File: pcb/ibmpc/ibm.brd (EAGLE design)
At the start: 104 x 74 mm, 40 parts, among them J2 ATX24RH

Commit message: working on new version
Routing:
- net N$3: track 133.6 -> 132.5 mm
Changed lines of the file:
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@@
 <layer number="14" name="Route14" color="22" fill="1" visible="no" active="no"/>
 <layer number="15" name="Route15" color="23" fill="1" visible="no" active="no"/>
-<layer number="16" name="Bottom" color="1" fill="1" visible="yes" active="yes"/>
+<layer number="16" name="Bottom" color="1" fill="1" visible="no" active="yes"/>
 <layer number="17" name="Pads" color="2" fill="1" visible="yes" active="yes"/>
 <layer number="18" name="Vias" color="2" fill="1" visible="yes" active="yes"/>
@@
 <layer number="22" name="bPlace" color="7" fill="1" visible="no" active="yes"/>
 <layer number="23" name="tOrigins" color="15" fill="1" visible="yes" active="yes"/>
-<layer number="24" name="bOrigins" color="15" fill="1" visible="yes" active="yes"/>
+<layer number="24" name="bOrigins" color="15" fill="1" visible="no" active="yes"/>
 <layer number="25" name="tNames" color="7" fill="1" visible="no" active="yes"/>
 <layer number="26" name="bNames" color="7" fill="1" visible="no" active="yes"/>
@@
 <layer number="38" name="bTest" color="7" fill="1" visible="no" active="yes"/>
 <layer number="39" name="tKeepout" color="4" fill="11" visible="yes" active="yes"/>
-<layer number="40" name="bKeepout" color="1" fill="11" visible="yes" active="yes"/>
+<layer number="40" name="bKeepout" color="1" fill="11" visible="no" active="yes"/>
 <layer number="41" name="tRestrict" color="4" fill="10" visible="yes" active="yes"/>
-<layer number="42" name="bRestrict" color="1" fill="10" visible="yes" active="yes"/>
+<layer number="42" name="bRestrict" color="1" fill="10" visible="no" active="yes"/>
 <layer number="43" name="vRestrict" color="2" fill="10" visible="no" active="yes"/>
 <layer number="44" name="Drills" color="7" fill="1" visible="no" active="yes"/>
@@
 <wire x1="94.234" y1="45.212" x2="94.234" y2="51.435" width="0.3048" layer="16"/>
 <wire x1="92.642" y1="43.62" x2="94.234" y2="45.212" width="0.3048" layer="16"/>
-<wire x1="88.821" y1="64.446" x2="88.821" y2="63.452" width="0.3048" layer="16"/>
-<wire x1="88.821" y1="63.452" x2="90.424" y2="61.849" width="0.3048" layer="16"/>
-<wire x1="90.424" y1="61.849" x2="92.456" y2="61.849" width="0.3048" layer="16"/>
-<wire x1="94.234" y1="60.071" x2="94.234" y2="51.435" width="0.3048" layer="16"/>
-<wire x1="92.456" y1="61.849" x2="94.234" y2="60.071" width="0.3048" layer="16"/>
+<wire x1="88.821" y1="64.446" x2="88.821" y2="63.706" width="0.3048" layer="16"/>
+<wire x1="94.234" y1="58.293" x2="94.234" y2="51.435" width="0.3048" layer="16"/>
+<wire x1="88.821" y1="63.706" x2="94.234" y2="58.293" width="0.3048" layer="16"/>
 <wire x1="43.688" y1="52.451" x2="77.089" y2="52.451" width="0.3048" layer="16"/>
 <wire x1="77.089" y1="52.451" x2="78.105" y2="51.435" width="0.3048" layer="16"/>

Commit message: working on new version
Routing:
- net GND: track 63.2 -> 62.2 mm
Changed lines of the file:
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@@
 <layer number="14" name="Route14" color="22" fill="1" visible="no" active="no"/>
 <layer number="15" name="Route15" color="23" fill="1" visible="no" active="no"/>
-<layer number="16" name="Bottom" color="1" fill="1" visible="no" active="yes"/>
+<layer number="16" name="Bottom" color="1" fill="1" visible="yes" active="yes"/>
 <layer number="17" name="Pads" color="2" fill="1" visible="yes" active="yes"/>
 <layer number="18" name="Vias" color="2" fill="1" visible="yes" active="yes"/>
 <layer number="19" name="Unrouted" color="6" fill="1" visible="yes" active="yes"/>
 <layer number="20" name="Dimension" color="24" fill="1" visible="yes" active="yes"/>
-<layer number="21" name="tPlace" color="7" fill="1" visible="no" active="yes"/>
-<layer number="22" name="bPlace" color="7" fill="1" visible="no" active="yes"/>
+<layer number="21" name="tPlace" color="7" fill="1" visible="yes" active="yes"/>
+<layer number="22" name="bPlace" color="7" fill="1" visible="yes" active="yes"/>
 <layer number="23" name="tOrigins" color="15" fill="1" visible="yes" active="yes"/>
-<layer number="24" name="bOrigins" color="15" fill="1" visible="no" active="yes"/>
-<layer number="25" name="tNames" color="7" fill="1" visible="no" active="yes"/>
-<layer number="26" name="bNames" color="7" fill="1" visible="no" active="yes"/>
-<layer number="27" name="tValues" color="7" fill="1" visible="no" active="yes"/>
-<layer number="28" name="bValues" color="7" fill="1" visible="no" active="yes"/>
+<layer number="24" name="bOrigins" color="15" fill="1" visible="yes" active="yes"/>
+<layer number="25" name="tNames" color="7" fill="1" visible="yes" active="yes"/>
+<layer number="26" name="bNames" color="7" fill="1" visible="yes" active="yes"/>
+<layer number="27" name="tValues" color="7" fill="1" visible="yes" active="yes"/>
+<layer number="28" name="bValues" color="7" fill="1" visible="yes" active="yes"/>
 <layer number="29" name="tStop" color="7" fill="3" visible="no" active="yes"/>
 <layer number="30" name="bStop" color="7" fill="6" visible="no" active="yes"/>
@@
 <layer number="38" name="bTest" color="7" fill="1" visible="no" active="yes"/>
 <layer number="39" name="tKeepout" color="4" fill="11" visible="yes" active="yes"/>
-<layer number="40" name="bKeepout" color="1" fill="11" visible="no" active="yes"/>
+<layer number="40" name="bKeepout" color="1" fill="11" visible="yes" active="yes"/>
 <layer number="41" name="tRestrict" color="4" fill="10" visible="yes" active="yes"/>
-<layer number="42" name="bRestrict" color="1" fill="10" visible="no" active="yes"/>
+<layer number="42" name="bRestrict" color="1" fill="10" visible="yes" active="yes"/>
 <layer number="43" name="vRestrict" color="2" fill="10" visible="no" active="yes"/>
 <layer number="44" name="Drills" color="7" fill="1" visible="no" active="yes"/>
@@
 <layer number="49" name="Reference" color="7" fill="1" visible="no" active="yes"/>
 <layer number="50" name="dxf" color="7" fill="1" visible="no" active="no"/>
-<layer number="51" name="tDocu" color="7" fill="1" visible="no" active="yes"/>
-<layer number="52" name="bDocu" color="7" fill="1" visible="no" active="yes"/>
+<layer number="51" name="tDocu" color="7" fill="1" visible="yes" active="yes"/>
+<layer number="52" name="bDocu" color="7" fill="1" visible="yes" active="yes"/>
 <layer number="53" name="tGND_GNDA" color="7" fill="1" visible="no" active="no"/>
 <layer number="54" name="bGND_GNDA" color="7" fill="1" visible="no" active="no"/>
@@
 <wire x1="104" y1="10.795" x2="100.825" y2="7.62" width="0" layer="20" curve="-90"/>
 <wire x1="100.825" y1="7.62" x2="81" y2="7.62" width="0" layer="20"/>
-<text x="41.3926" y="4.0764" size="2.54" layer="25" distance="35" align="center">IBM PC PicoPSU Adaptor
+<text x="73.2696" y="12.9664" size="2.54" layer="25" distance="35" align="center">IBM PC PicoPSU Adaptor
 dekuNukem 2023</text>
 <text x="83.608" y="45.184" size="2.54" layer="25" rot="R180" align="center">GND</text>
 <text x="34.218" y="71.93" size="2.1844" layer="25" distance="35" align="center">FUSE 7.5A MAX</text>
-<text x="52.3746" y="22.3784" size="3.175" layer="25" distance="35" align="center">picoRC.com</text>
+<text x="53.0096" y="22.1244" size="3.175" layer="25" distance="35" align="center">picoRC.com</text>
 <text x="38.529" y="26.012" size="1.4224" layer="25" align="center">GND</text>
 <text x="38.275" y="23.615" size="1.4224" layer="25" align="center">-12</text>
@@
 </element>
 <element name="C17" library="capacitor-wima" library_urn="urn:adsk.eagle:library:116" package="C5B2.5" package3d_urn="urn:adsk.eagle:package:5426/1" value="" x="35.733" y="34.474" smashed="yes" rot="R180">
-<attribute name="NAME" x="31.947" y="31.796" size="1.27" layer="25" ratio="10"/>
+<attribute name="NAME" x="31.947" y="31.542" size="1.27" layer="25" ratio="10"/>
 <attribute name="POPULARITY" value="10" x="35.733" y="34.474" size="1.778" layer="27" rot="R180" display="off"/>
 <attribute name="VALUE" x="37.765" y="37.268" size="1.27" layer="27" ratio="10" rot="R180"/>
@@
 <via x="2.413" y="11.43" extent="1-16" drill="1"/>
 <via x="2.413" y="9.398" extent="1-16" drill="1"/>
-<wire x1="2.413" y1="11.43" x2="2.413" y2="9.398" width="2.54" layer="16"/>
-<wire x1="2.413" y1="9.398" x2="2.413" y2="8.382" width="2.54" layer="16"/>
-<wire x1="2.387" y1="4" x2="2.387" y2="7.594" width="1.016" layer="16"/>
-<wire x1="2.387" y1="7.594" x2="2.413" y2="7.62" width="1.016" layer="16"/>
-<wire x1="2.413" y1="7.62" x2="2.413" y2="9.398" width="1.016" layer="16"/>
 <contactref element="C12" pad="-"/>
 <contactref element="C13" pad="2"/>
@@
 <vertex x="10.668" y="14.224"/>
 </polygon>
+<wire x1="2.413" y1="11.43" x2="2.413" y2="9.398" width="2.54" layer="16"/>
+<wire x1="2.387" y1="4" x2="2.387" y2="9.372" width="1.524" layer="16"/>
+<wire x1="2.387" y1="9.372" x2="2.413" y2="9.398" width="1.524" layer="16"/>
 </signal>
 <signal name="+5V">

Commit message: working on new version
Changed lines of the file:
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@@
 <text x="83.608" y="45.184" size="2.54" layer="25" rot="R180" align="center">GND</text>
 <text x="34.218" y="71.93" size="2.1844" layer="25" distance="35" align="center">FUSE 7.5A MAX</text>
-<text x="53.0096" y="22.1244" size="3.175" layer="25" distance="35" align="center">picoRC.com</text>
+<text x="25.1966" y="11.2024" size="3.175" layer="25" distance="35" align="center">picoRC.com</text>
 <text x="38.529" y="26.012" size="1.4224" layer="25" align="center">GND</text>
 <text x="38.275" y="23.615" size="1.4224" layer="25" align="center">-12</text>

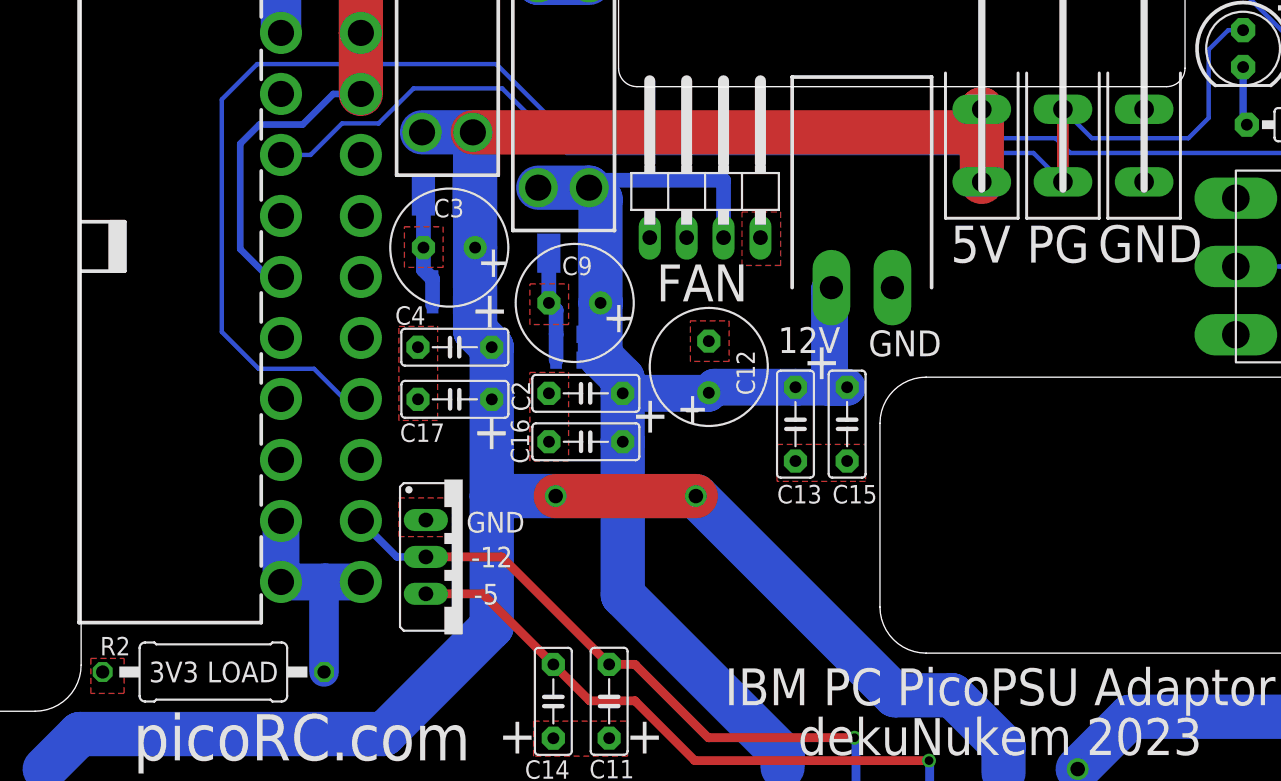
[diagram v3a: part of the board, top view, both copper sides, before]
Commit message: added 12V load resistor and blade
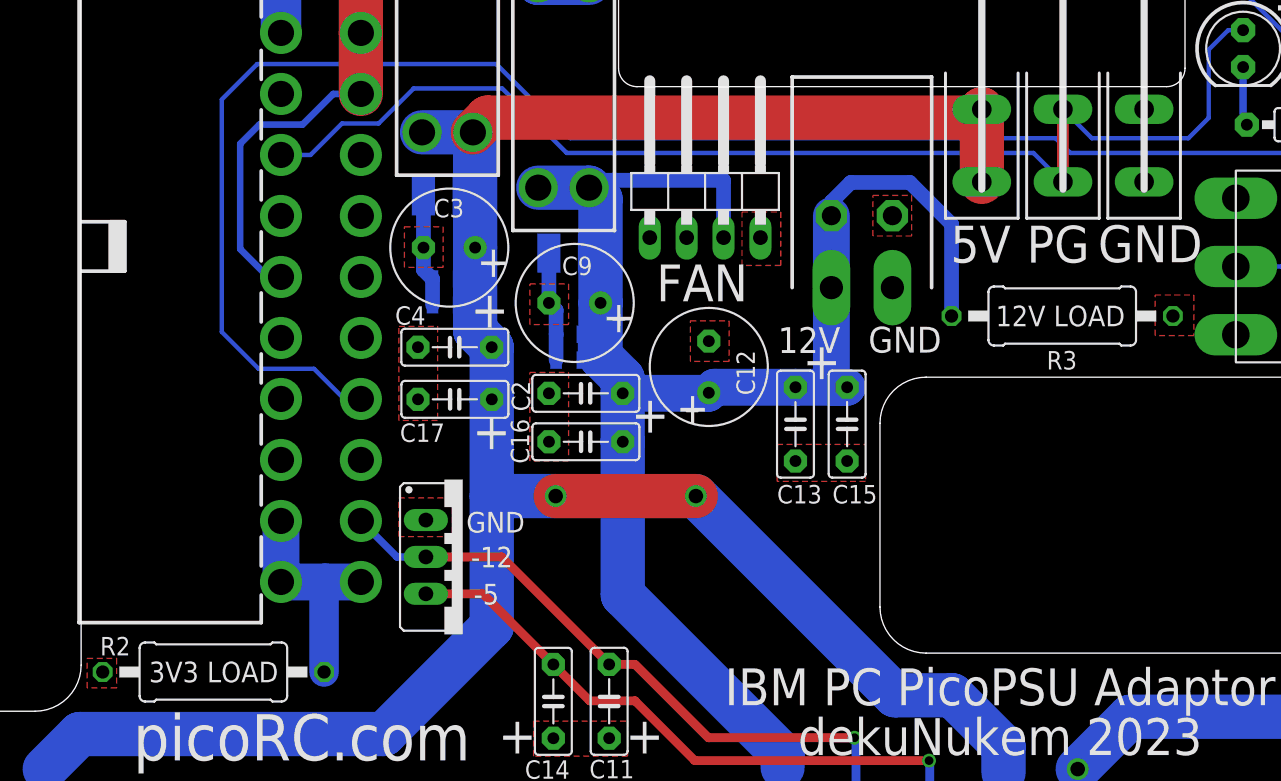
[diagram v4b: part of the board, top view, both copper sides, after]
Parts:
- added R3: (no value), adafruit_changed:0411/15
- added TP1, TP2: TPPAD1-13, testpad:P1-13
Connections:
- net +12V: now also R3.2, TP2.TP
- net GND: now also R3.1, TP1.TP
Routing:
- net +12V: track 99.4 -> 121.4 mm
- net +5V: track 176.9 -> 176.3 mm
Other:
- board text added: "12V LOAD"
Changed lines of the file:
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@@
 <text x="52.753" y="42.49" size="2.54" layer="25" align="center">FAN</text>
 <text x="60.119" y="38.553" size="1.778" layer="25" align="center">12V</text>
-<text x="66.717" y="38.326" size="1.778" layer="25" rot="R180" align="center">GND</text>
+<text x="66.717" y="38.58" size="1.778" layer="25" rot="R180" align="center">GND</text>
 <rectangle x1="69.469" y1="48.006" x2="74.549" y2="55.753" layer="41"/>
 <rectangle x1="75.184" y1="48.006" x2="80.264" y2="55.753" layer="41"/>
@@
 <text x="47.019" y="40.185" size="2.1844" layer="25" align="center">+</text>
 <text x="38.383" y="43.995" size="2.1844" layer="25" align="center">+</text>
+<text x="77.416" y="40.212" size="1.4224" layer="25" rot="R180" align="center">12V LOAD</text>
 </plain>
 <attributes>
@@
 <attribute name="VALUE" x="59.944" y="34.798" size="1.27" layer="27" ratio="10" rot="R270"/>
 </element>
+<element name="R3" library="adafruit_changed" package="0411/15" value="" x="77.548" y="40.21" smashed="yes" rot="R180">
+<attribute name="NAME" x="78.564" y="37.797" size="1.27" layer="25" ratio="10" rot="R180"/>
+<attribute name="VALUE" x="81.1294" y="40.845" size="1.27" layer="27" ratio="10" rot="R180"/>
+</element>
+<element name="TP2" library="testpad" library_urn="urn:adsk.eagle:library:385" package="P1-13" package3d_urn="urn:adsk.eagle:package:27946/1" value="TPPAD1-13" x="61.654" y="47.117" smashed="yes">
+<attribute name="POPULARITY" value="12" x="61.654" y="47.117" size="1.778" layer="27" display="off"/>
+<attribute name="TP_SIGNAL_NAME" value="" x="61.654" y="47.117" size="1.778" layer="27" display="off"/>
+</element>
+<element name="TP1" library="testpad" library_urn="urn:adsk.eagle:library:385" package="P1-13" package3d_urn="urn:adsk.eagle:package:27946/1" value="TPPAD1-13" x="65.854" y="47.117" smashed="yes">
+<attribute name="POPULARITY" value="12" x="65.854" y="47.117" size="1.778" layer="27" display="off"/>
+<attribute name="TP_SIGNAL_NAME" value="" x="65.854" y="47.117" size="1.778" layer="27" display="off"/>
+</element>
 </elements>
 <signals>
@@
 </polygon>
 <polygon width="0.1524" layer="1" thermals="no">
-<vertex x="10.668" y="16.637"/>
-<vertex x="12.954" y="16.637"/>
-<vertex x="12.954" y="14.224"/>
-<vertex x="10.668" y="14.224"/>
+<vertex x="10.414" y="16.637"/>
+<vertex x="12.446" y="16.637"/>
+<vertex x="12.446" y="14.605"/>
+<vertex x="10.414" y="14.605"/>
 </polygon>
 <wire x1="2.413" y1="11.43" x2="2.413" y2="9.398" width="2.54" layer="16"/>
 <wire x1="2.387" y1="4" x2="2.387" y2="9.372" width="1.524" layer="16"/>
 <wire x1="2.387" y1="9.372" x2="2.413" y2="9.398" width="1.524" layer="16"/>
+<contactref element="R3" pad="1"/>
+<contactref element="TP1" pad="TP"/>
+<polygon width="0.1524" layer="1" thermals="no">
+<vertex x="64.516" y="48.514"/>
+<vertex x="67.183" y="48.514"/>
+<vertex x="67.183" y="45.72"/>
+<vertex x="64.516" y="45.72"/>
+</polygon>
+<polygon width="0.1524" layer="1" thermals="no">
+<vertex x="83.947" y="41.656"/>
+<vertex x="86.614" y="41.656"/>
+<vertex x="86.614" y="38.862"/>
+<vertex x="83.947" y="38.862"/>
+</polygon>
 </signal>
 <signal name="+5V">
@@
 <wire x1="7.493" y1="9.017" x2="7.493" y2="4.026" width="1.27" layer="16"/>
 <wire x1="7.493" y1="4.026" x2="7.467" y2="4" width="1.27" layer="16"/>
-<wire x1="36.97" y1="52.856" x2="72.009" y2="52.856" width="3.048" layer="1"/>
-<wire x1="72.009" y1="52.856" x2="72.009" y2="54.443" width="3.048" layer="1"/>
+<wire x1="72.009" y1="53.872" x2="37.986" y2="53.872" width="3.048" layer="1"/>
+<wire x1="36.97" y1="52.856" x2="37.986" y2="53.872" width="3.048" layer="1"/>
+<wire x1="72.009" y1="53.872" x2="72.009" y2="54.443" width="3.048" layer="1"/>
 <wire x1="72.009" y1="54.443" x2="72.009" y2="49.443" width="3.048" layer="1"/>
 <wire x1="38.273" y1="34.474" x2="38.273" y2="27.813" width="3.048" layer="16"/>
@@
 <contactref element="C13" pad="1"/>
 <contactref element="C15" pad="1"/>
-<wire x1="62.738" y1="35.306" x2="61.527" y2="35.306" width="2.54" layer="16"/>
+<wire x1="62.738" y1="35.306" x2="61.654" y2="35.306" width="2.54" layer="16"/>
 <wire x1="62.738" y1="35.306" x2="59.182" y2="35.306" width="2.54" layer="16"/>
 <wire x1="47.285" y1="34.887" x2="53.175" y2="34.887" width="2.54" layer="16"/>
@@
 <wire x1="53.213" y1="34.925" x2="53.594" y2="35.306" width="2.54" layer="16"/>
 <wire x1="59.182" y1="35.306" x2="53.594" y2="35.306" width="2.54" layer="16"/>
-<wire x1="61.654" y1="42.164" x2="61.527" y2="42.037" width="2.54" layer="16"/>
-<wire x1="61.527" y1="42.037" x2="61.527" y2="35.306" width="2.54" layer="16"/>
+<wire x1="61.654" y1="42.037" x2="61.654" y2="35.306" width="2.54" layer="16"/>
 <wire x1="45.002" y1="44.539" x2="45.761" y2="43.78" width="0.6096" layer="16"/>
 <wire x1="45.761" y1="43.78" x2="45.761" y2="41.11" width="0.6096" layer="16"/>
@@
 <wire x1="45.761" y1="40.21" x2="44.502" y2="38.951" width="0.6096" layer="16"/>
 <wire x1="44.502" y1="38.951" x2="44.502" y2="37.173" width="0.6096" layer="16"/>
+<contactref element="R3" pad="2"/>
+<contactref element="TP2" pad="TP"/>
+<wire x1="61.654" y1="42.164" x2="61.654" y2="47.117" width="2.54" layer="16"/>
+<wire x1="61.654" y1="47.117" x2="61.654" y2="48.065" width="1.016" layer="16"/>
+<wire x1="61.654" y1="48.065" x2="62.992" y2="49.403" width="1.016" layer="16"/>
+<wire x1="62.992" y1="49.403" x2="67.056" y2="49.403" width="1.016" layer="16"/>
+<wire x1="67.056" y1="49.403" x2="69.928" y2="46.531" width="1.016" layer="16"/>
+<wire x1="69.928" y1="46.531" x2="69.928" y2="40.21" width="1.016" layer="16"/>
+<wire x1="61.654" y1="42.037" x2="61.654" y2="42.164" width="0" layer="19" extent="16-16"/>
 </signal>
 <signal name="-12V">
